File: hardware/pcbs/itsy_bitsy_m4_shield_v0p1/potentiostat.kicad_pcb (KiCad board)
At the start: 2 copper layers, 144.8 x 88.9 mm, 141 parts, among them K1 Conn_01x03, P1 Conn_01x02, P10 Conn_01x02, P11 Conn_01x02, P12 Conn_01x02, P13 Conn_02x05_Odd_Even, P14 Conn_02x05_Odd_Even, P15 Conn_02x02_Odd_Even, P16 Conn_02x02_Odd_Even, P17 Conn_01x02, P18 Conn_01x02, P19 Conn_01x02, P2 Conn_01x02, P20 Conn_01x02, P21 Conn_01x02, P22 Conn_01x02, P3 Conn_01x02, P4 Conn_01x02, P5 Conn_01x02, P6 Conn_01x02, P7 Conn_01x02, P8 Conn_01x02, P9 Conn_01x02, U1 74HC138, U10 REF33XX, U11 OP07, U12 OP07, U13 OP07, U14 OP07, U15 OP07, U16 OP07, U17 OP07, U18 OP07, U19 74HC138, U2 ITSY_BITSY_M4, U20 OP07, U21 74HC138, U3 DG411xY, U4 DG411xY, U5 DG411xY, U6 MEA1D05XXSC, U7 DG411xY, U8 DG411xY, U9 TL072

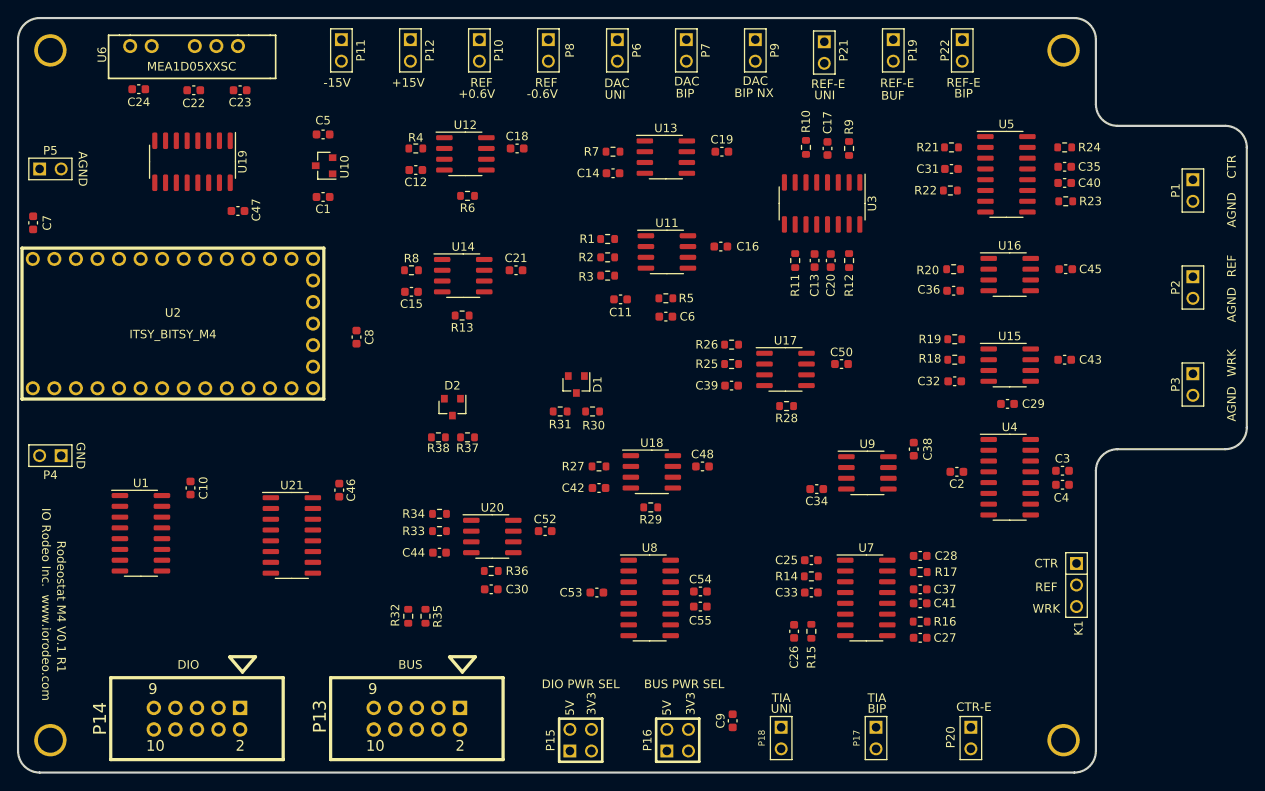
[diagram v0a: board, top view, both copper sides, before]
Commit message: Added initial routing of M4 version.
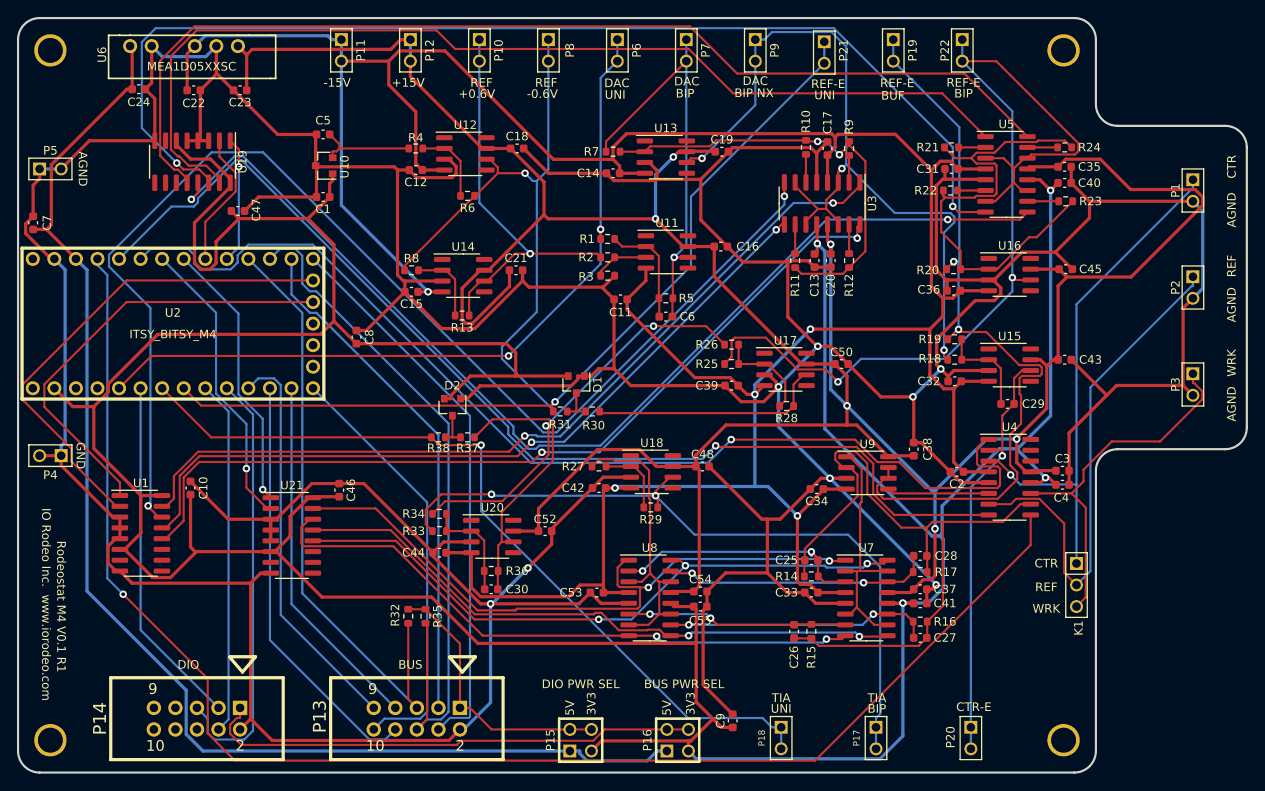
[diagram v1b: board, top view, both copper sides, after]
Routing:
- net /GND: track 0.00 -> 798.4 mm, vias 0 -> 8
- net /3V3: track 0.00 -> 454.2 mm, vias 0 -> 4
- net /-15V: track 0.00 -> 374.9 mm, vias 0 -> 5
- net /+15V: track 0.00 -> 368.6 mm, vias 0 -> 6
- net /SW_WRK_ELECT: track 0.00 -> 173.6 mm, vias 0 -> 1
- net /5V: track 0.00 -> 152.7 mm
- net /SW_GAIN_2X: track 0.00 -> 145.9 mm, vias 0 -> 2
- net /SW_GAIN_INV_2X: track 0.00 -> 134.1 mm, vias 0 -> 2
- net /SW_GAIN_INV_5X: track 0.00 -> 129.2 mm, vias 0 -> 2
- net /SW_REF_ELECT: track 0.00 -> 128.8 mm, vias 0 -> 1
- net /SW_CTR_ELECT: track 0.00 -> 127.8 mm, vias 0 -> 1
- net /SW_GAIN_INV_10X: track 0.00 -> 125.2 mm
- net /SW_GAIN_INV_1X: track 0.00 -> 121.0 mm
- net /REF_NEG_0V6: track 0.00 -> 119.5 mm, vias 0 -> 3
- net /REF_ELECT_BIP: track 0.00 -> 116.1 mm, vias 0 -> 2
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
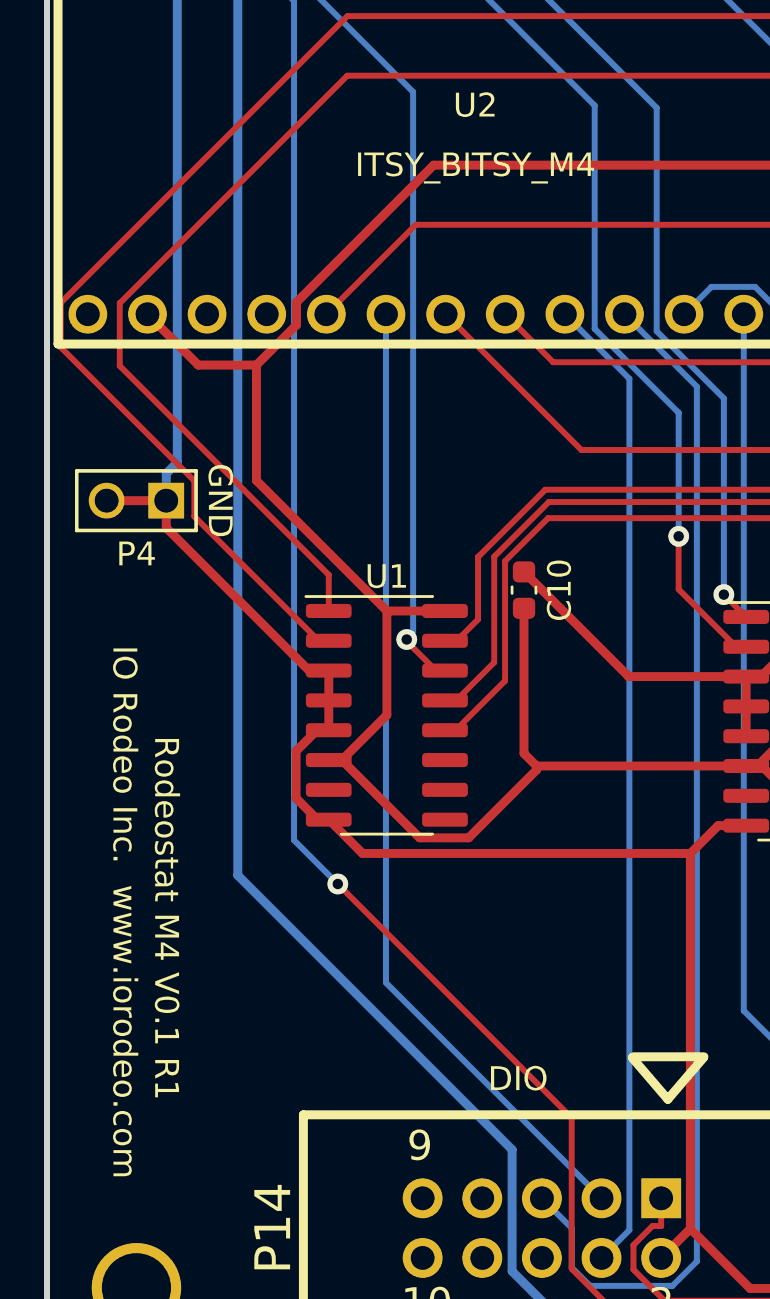
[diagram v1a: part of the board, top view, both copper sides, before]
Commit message: Created gerber files for itsy bitsy MX shield.
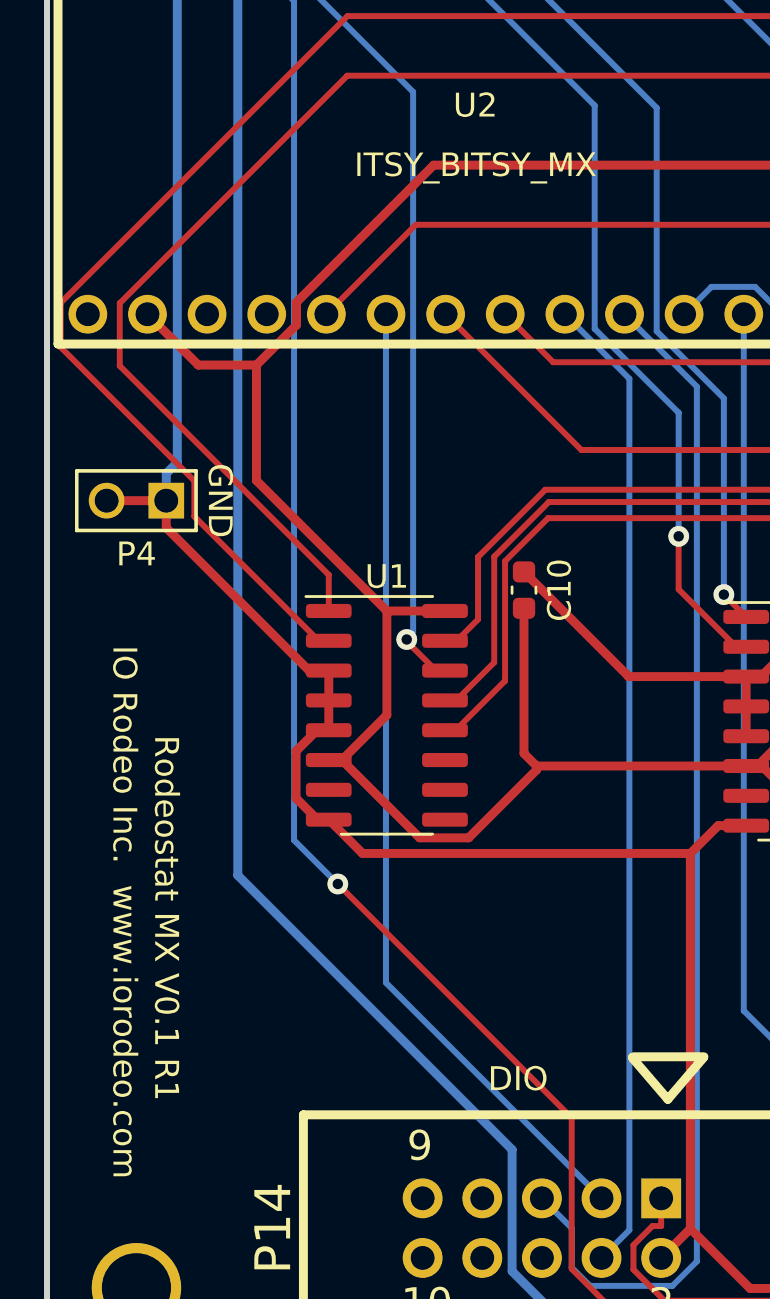
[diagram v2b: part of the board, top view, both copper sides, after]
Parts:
- U2: value ITSY_BITSY_M4 -> ITSY_BITSY_MX
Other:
- board text added: "Rodeostat MX V0.1 R1"
- board text removed: "Rodeostat M4 V0.1 R1"
